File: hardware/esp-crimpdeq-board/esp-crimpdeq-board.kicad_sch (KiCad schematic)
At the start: 60 parts, among them J1 USB4105-GF-A, Q1 DMG3415U, SW1 SW_Push, SW2 SW_Push, SW3 SW_Wuerth_450301014042, U1 SHTC3, U2 ICM-42670-P, U3 ESP32-C3-MINI-1, U5 SY8088, U6 MCP73831T-2ACI/OT, Y1 32.768Hz

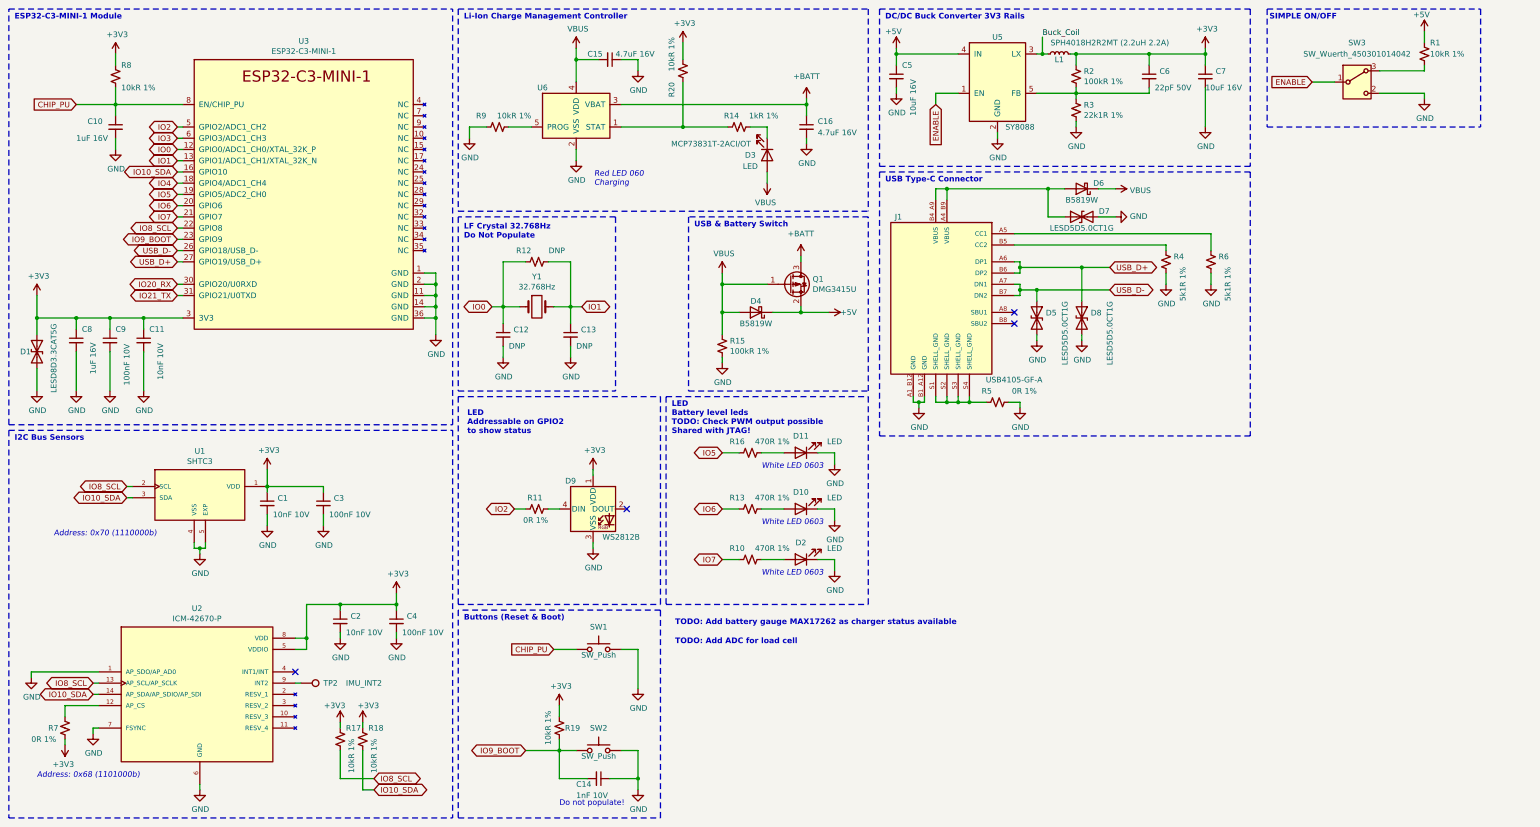
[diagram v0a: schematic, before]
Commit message: Updated espressif kicad libraries and removed some unecessary libs
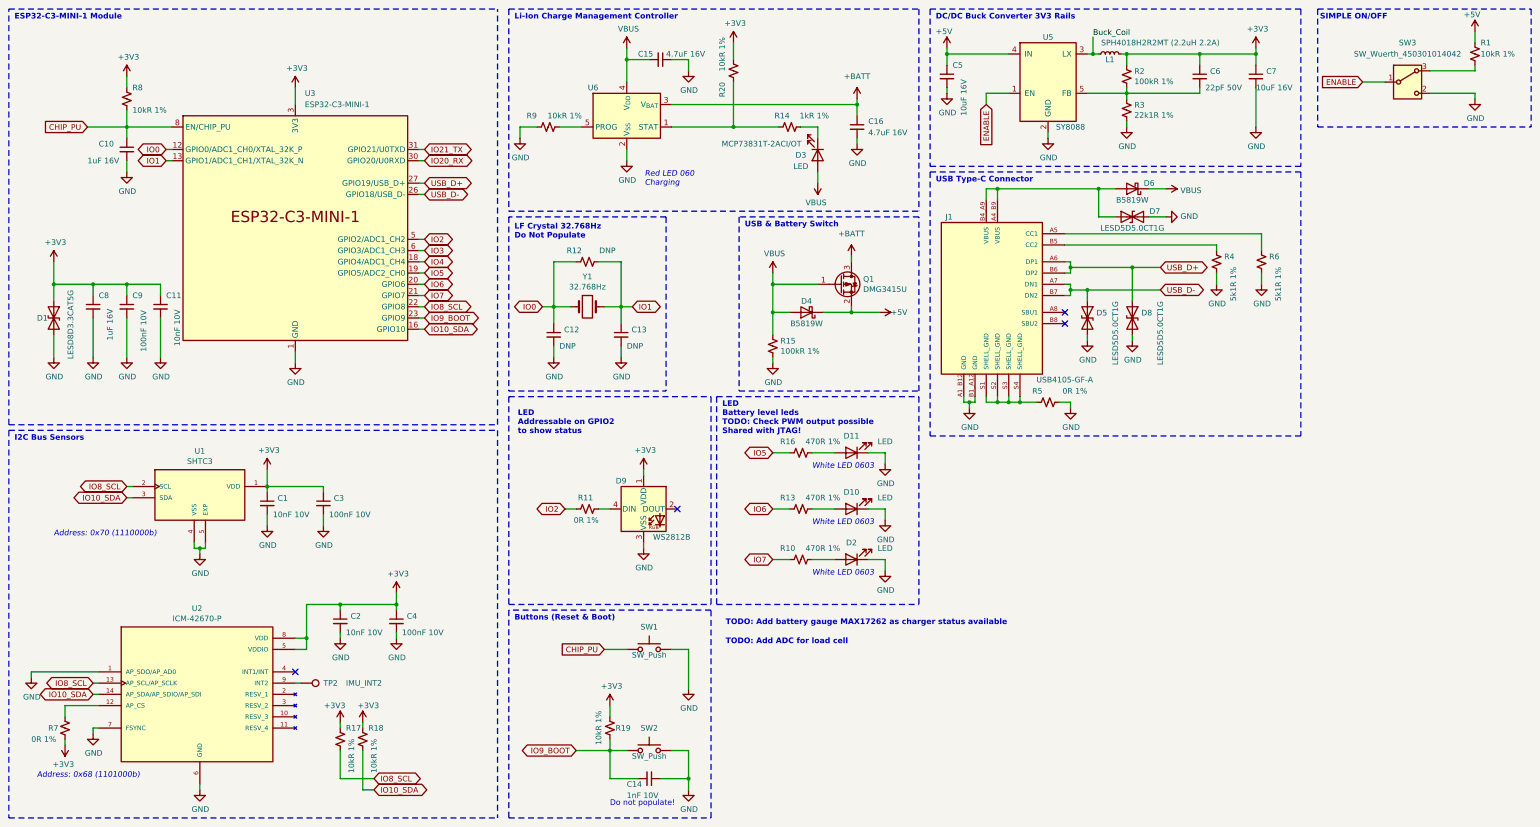
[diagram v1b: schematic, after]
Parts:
- removed U3: ESP32-C3-MINI-1, Espressif:ESP32-C3-MINI-1, symbol Espressif:ESP32-C3-MINI-1
- added U3: ESP32-C3-MINI-1, PCM_Espressif:ESP32-C3-MINI-1, symbol PCM_Espressif:ESP32-C3-MINI-1
- D9: footprint LED_SMD:LED_SK6812MINI_PLCC4_3.5x3.5mm_P1.75mm -> LED_SMD:LED_WS2812B_PLCC4_5.0x5.0mm_P3.2mm
- J1: footprint Rust_Board:GCT_USB4105-GF-A -> GCT_USB4105-GF-A
- U1: footprint Rust_Board:SON100P200X200X80-5N -> SON100P200X200X80-5N
- U2: footprint Rust_Board:IC_ICM-42670-P -> IC_ICM-42670-P
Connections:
- net +3V3: now also U3.3 (3V3)
- net CHIP_PU: now also U3.8 (EN/CHIP_PU)
- net GND: now also U3.1 (GND), U3.11 (GND), U3.14 (GND), U3.2 (GND), U3.36 (GND), U3.37 (GND), U3.38 (GND), U3.39 (GND), U3.40 (GND), U3.41 (GND), U3.42 (GND), U3.43 (GND), U3.44 (GND), U3.45 (GND), U3.46 (GND), U3.47 (GND), U3.48 (GND), U3.49 (GND), U3.50 (GND), U3.51 (GND), U3.52 (GND), U3.53 (GND)
- net IO0: now also U3.12 (GPIO0/ADC1_CH0/XTAL_32K_P)
- net IO1: now also U3.13 (GPIO1/ADC1_CH1/XTAL_32K_N)
- net IO10_SDA: now also U3.16 (GPIO10)
- net IO2: now also U3.5 (GPIO2/ADC1_CH2)
- net IO20_RX: now also U3.30 (GPIO20/U0RXD)
- net IO21_TX: now also U3.31 (GPIO21/U0TXD)
- net IO3: now also U3.6 (GPIO3/ADC1_CH3)
- net IO4: now also U3.18 (GPIO4/ADC1_CH4)
- net IO5: now also U3.19 (GPIO5/ADC2_CH0)
- net IO6: now also U3.20 (GPIO6)
- net IO7: now also U3.21 (GPIO7)
- net IO8_SCL: now also U3.22 (GPIO8)
- net IO9_BOOT: now also U3.23 (GPIO9)
- net USB_D+: now also U3.27 (GPIO19/USB_D+)
- net USB_D-: now also U3.26 (GPIO18/USB_D-)
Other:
- moved on the sheet: C10, C11, C12, C13, C14, C15, C16, C5, C6, C7, C8, C9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

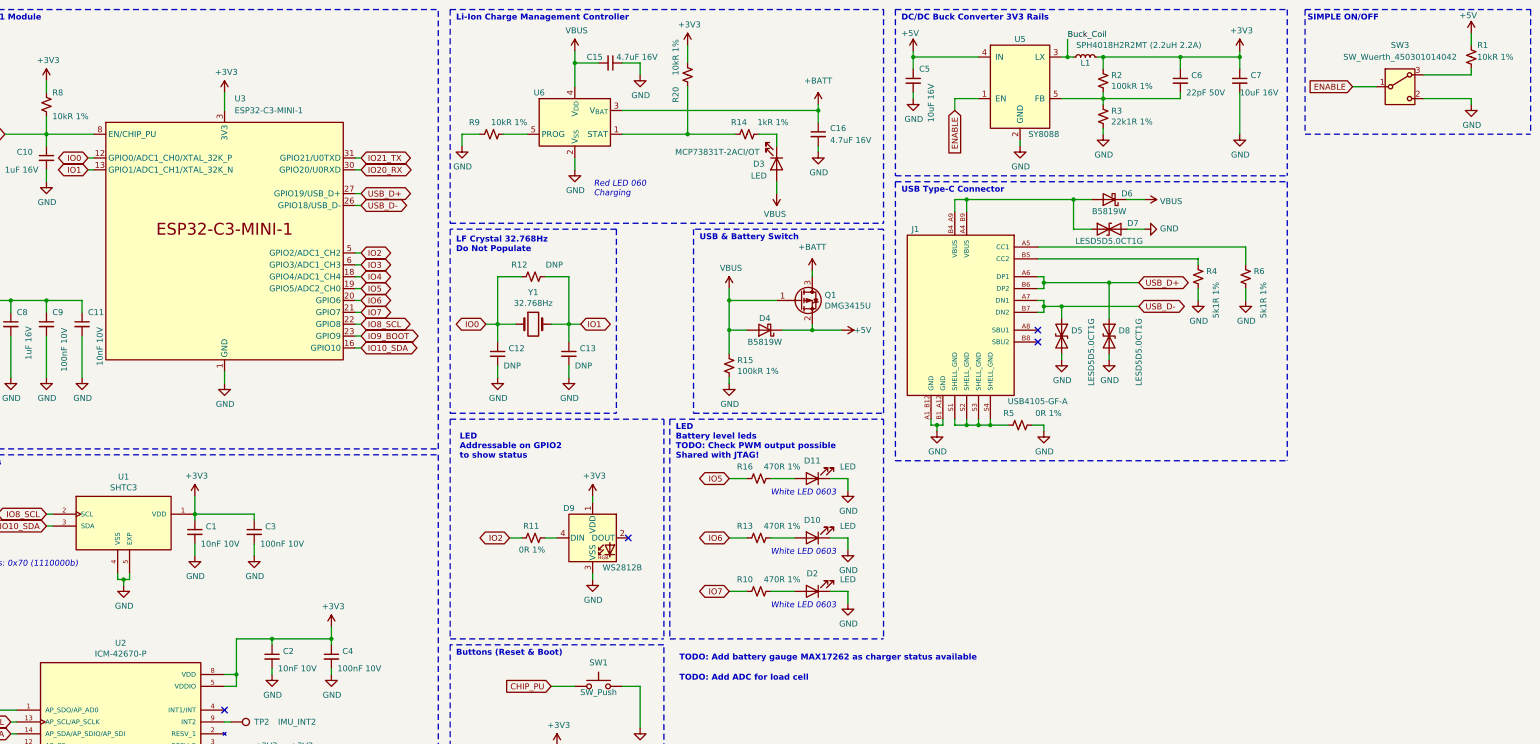
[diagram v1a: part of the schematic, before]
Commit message: Changed link libraries
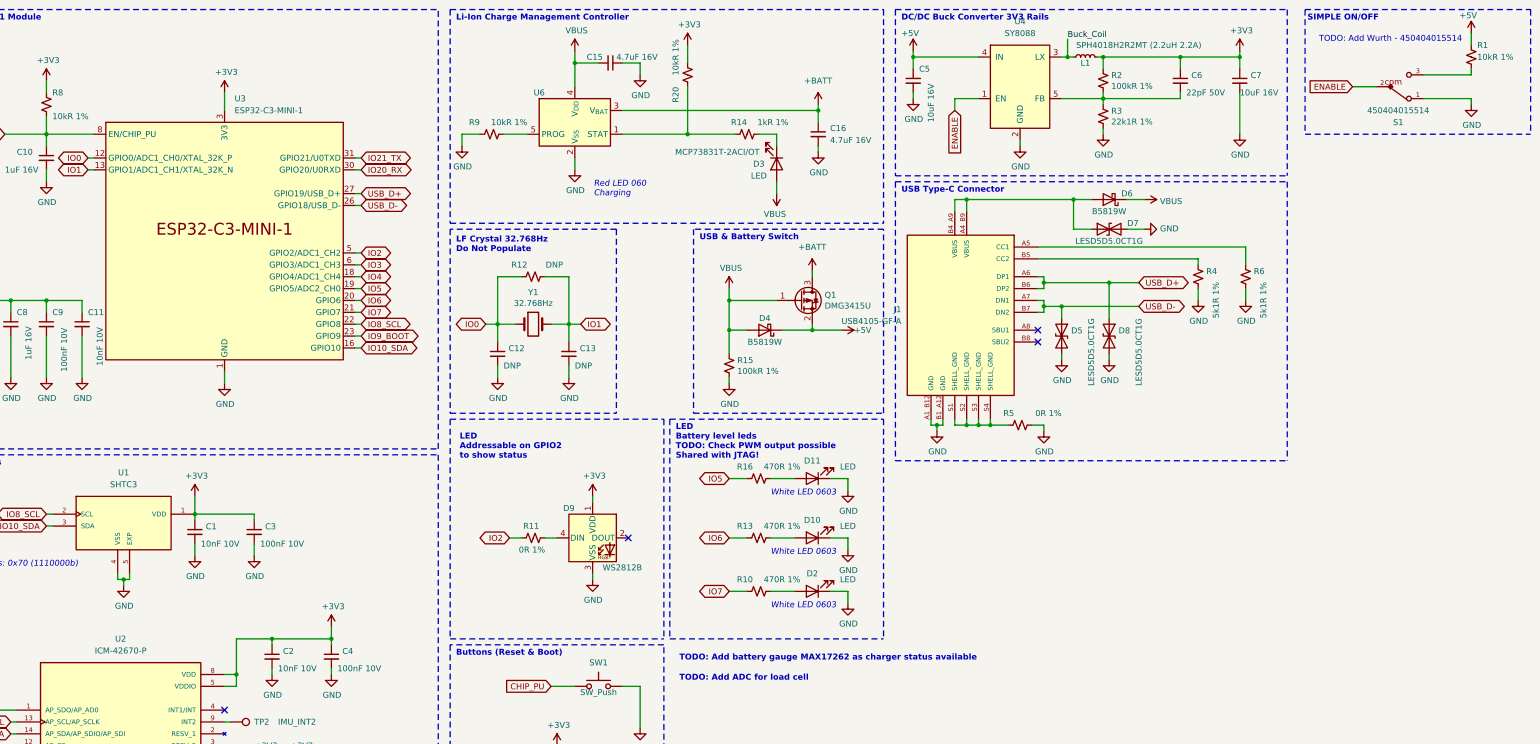
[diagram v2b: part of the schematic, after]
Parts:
- removed J1: USB4105-GF-A, GCT_USB4105-GF-A, symbol Rust_Board:USB4105-GF-A
- removed SW3: SW_Wuerth_450301014042, Button_Switch_THT:SW_Slide-03_Wuerth-WS-SLTV_10x2.5x6.4_P2.54mm, symbol Switch:SW_Wuerth_450301014042
- removed U1: SHTC3, SON100P200X200X80-5N, symbol Rust_Board:SHTC3
- removed U2: ICM-42670-P, IC_ICM-42670-P, symbol Rust_Board:ICM-42670-P
- removed U5: SY8088, Package_TO_SOT_SMD:SOT-23-5, symbol Rust_Board:SY8088
- added J1: USB4105-GF-A, PCM_GCT:GCT_USB4105-GF-A, symbol PCM_GCT:USB4105-GF-A
- added S1: 450404015514, PCM_Wurth_Elektronik:450404015514, symbol PCM_Wurth_Elektronik:450404015514
- added U1: SHTC3, PCM_Sensirion:SON100P200X200X80-5N, symbol PCM_Sensirion:SHTC3
- added U2: ICM-42670-P, PCM_TDK_InvenSense:IC_ICM-42670-P, symbol PCM_TDK_InvenSense:ICM-42670-P
- added U4: SY8088, Package_TO_SOT_SMD:SOT-23-5, symbol PCM_Silergy:SY8088
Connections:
- net +3V3: now also U1.1 (VDD), U2.5 (VDDIO), U2.8 (VDD)
- net +5V: now also U4.4 (IN)
- net Buck_Coil: now also U4.3 (LX)
- net ENABLE: now also S1.2, U4.1 (EN)
- net GND: now also J1.A1_B12 (GND), J1.B1_A12 (GND), S1.1, U1.4 (VSS), U1.5 (EXP), U2.1 (AP_SDO/AP_AD0), U2.6 (GND), U2.7 (FSYNC), U4.2 (GND)
- net IO10_SDA: now also U1.3 (SDA), U2.14 (AP_SDA/AP_SDIO/AP_SDI)
- net IO8_SCL: now also U1.2 (SCL), U2.13 (AP_SCL/AP_SCLK)
- net USB_D+: now also J1.A6 (DP1), J1.B6 (DP2)
- net USB_D-: now also J1.A7 (DN1), J1.B7 (DN2)
- net at R7.1: now also U2.12 (AP_CS)
- net at TP2.1: now also U2.9 (INT2)
- net at C6.2, R2.2, R3.1: now also U4.5 (FB)
- net at D6.2 (A), D7.1 (A1): now also J1.A4_B9 (VBUS), J1.B4_A9 (VBUS)
- net at R6.1: now also J1.A5 (CC1)
- net at R4.1: now also J1.B5 (CC2)
- net at R5.1: now also J1.S1 (SHELL_GND), J1.S2 (SHELL_GND), J1.S3 (SHELL_GND), J1.S4 (SHELL_GND)
- net at R1.2: now also S1.3
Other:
- note added: "TODO: Add Wurth - 450404015514"

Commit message: Added notes
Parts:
- added U5: HX711, Package_SO:SOP-16_3.9x9.9mm_P1.27mm, symbol Analog_ADC:HX711
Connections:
- net IO2: now also R14.1, R20.1, U6.1 (STAT)
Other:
- note added: "TODO: Add ADC for load cell. NAU7802. Pending temperature sensor. As reference ADS1262. Add pt100"
- note removed: "TODO: Add ADC for load cell"
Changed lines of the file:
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@@
 		)
 	)
-	(text "TODO: Add ADC for load cell"
+	(text "TODO: Add ADC for load cell. NAU7802. Pending temperature sensor. As reference ADS1262. Add pt100"
 		(exclude_from_sim no)
 		(at 174.752 157.734 0)
@@
 		)
 	)
+	(wire
+		(pts
+			(xy 176.53 40.64) (xy 176.53 46.99)
+		)
+		(stroke
+			(width 0)
+			(type default)
+		)
+	)
 	(polyline
 		(pts
@@
 		)
 	)
+	(global_label "IO3"
+		(shape bidirectional)
+		(at 237.49 127 0)
+		(fields_autoplaced yes)
+		(effects
+			(font
+				(size 1.27 1.27)
+			)
+			(justify left)
+		)
+		(property "Intersheetrefs" "${INTERSHEET_REFS}"
+			(at 243.9183 127 0)
+			(effects
+				(font
+					(size 1.27 1.27)
+				)
+				(justify left)
+				(hide yes)
+			)
+		)
+	)
 	(global_label "IO8_SCL"
 		(shape bidirectional)
@@
 		)
 	)
+	(global_label "IO2"
+		(shape bidirectional)
+		(at 176.53 46.99 270)
+		(fields_autoplaced yes)
+		(effects
+			(font
+				(size 1.27 1.27)
+			)
+			(justify right)
+		)
+		(property "Intersheetrefs" "${INTERSHEET_REFS}"
+			(at 176.53 53.4183 90)
+			(effects
+				(font
+					(size 1.27 1.27)
+				)
+				(justify right)
+				(hide yes)
+			)
+		)
+	)
 	(global_label "IO7"
 		(shape bidirectional)
@@
 		)
 		(property "Value" "MCP73831T-2ACI/OT"
-			(at 182.88 44.45 0)
+			(at 164.338 45.974 0)
 			(effects
 				(font
@@
 					(unit 1)
 				)
+			)
+		)
+	)
+	(symbol
+		(lib_id "Analog_ADC:HX711")
+		(at 50.8 227.33 0)
+		(unit 1)
+		(exclude_from_sim no)
+		(in_bom yes)
+		(on_board yes)
+		(dnp no)
+		(fields_autoplaced yes)
+		(property "Reference" "U5"
+			(at 52.9433 247.65 0)
+			(effects
+				(font
+					(size 1.27 1.27)
+				)
+				(justify left)
+			)
+		)
+		(property "Value" "HX711"
+			(at 52.9433 250.19 0)
+			(effects
+				(font
+					(size 1.27 1.27)
+				)
+				(justify left)
+			)
+		)
+		(property "Footprint" "Package_SO:SOP-16_3.9x9.9mm_P1.27mm"
+			(at 54.61 226.06 0)
+			(effects
+				(font
+					(size 1.27 1.27)
+				)
+				(hide yes)
+			)
+		)
+		(property "Datasheet" "https://web.archive.org/web/20220615044707/https://akizukidenshi.com/download/ds/avia/hx711.pdf"
+			(at 54.61 228.6 0)
+			(effects
+				(font
+					(size 1.27 1.27)
+				)
+				(hide yes)
+			)
+		)
+		(property "Description" "24-Bit Analog-to-Digital Converter (ADC) for Weight Scales"
+			(at 50.8 227.33 0)
+			(effects
+				(font
+					(size 1.27 1.27)
+				)
+				(hide yes)
+			)
+		)
+		(pin "11"
+		)
+		(pin "12"
+		)
+		(pin "9"
+		)
+		(pin "8"
+		)
+		(pin "7"
+		)
+		(pin "10"
+		)
+		(pin "2"
+		)
+		(pin "6"
+		)
+		(pin "1"
+		)
+		(pin "3"
+		)
+		(pin "4"
+		)
+		(pin "16"
+		)
+		(pin "5"
+		)
+		(pin "14"
+		)
+		(pin "15"
+		)
+		(pin "13"
+		)
+		(instances
+			(project ""
+				(path "/196a8dd5-5fd6-4c7f-ae4a-0104bd82e61b"
+					(reference "U5")
+					(unit 1)
+				)

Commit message: Added gauge
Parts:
- added C17: 0.47uF 16V, Capacitor_SMD:C_0603_1608Metric, symbol Device:C_Small
- added C18: 0.1uF 16V, Capacitor_SMD:C_0603_1608Metric, symbol Device:C_Small
- added U7: ~, Package_BGA:WLP-9_1.468x1.448mm_Layout3x3_P0.4mm, symbol PCM_Maxim:MAX17262
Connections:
- net +BATT: now also C18.1, U7.A2 (BATT); no longer C16.1, Q1.3 (D), U6.3 (V_{BAT})
- net GND: now also C17.2, C18.2, U7.C3 (GND/CSPL)
- net IO10_SDA: now also U7.C1 (SDA)
- net IO8_SCL: now also U7.B1 (SCL)
- new net: C17.1, U7.C2 (REG)
- new net +BATT_SYS: C16.1, Q1.3 (D), U6.3 (V_{BAT}), U7.B3 (SYS)
- no-connect marks 4 -> 6
